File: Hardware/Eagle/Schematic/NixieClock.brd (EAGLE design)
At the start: 256.5 x 112.7 mm, 10 parts

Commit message: Molex connectors in place.. use part 39-30-6147 on mouser
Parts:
- added X1, X2, X3, X4, X5, X6: 5566-14, con-molex:5566-14
- moved U$5 23.4 mm to (-41.9, 58.4)
- moved U$6 20.5 mm to (-16.5, 58.4)
- moved U$2 19.8 mm to (74.9, 44.5)
- moved U$7 19.3 mm to (8.89, 58.4)
- moved U$4 18.9 mm to (-27.9, 45.7)
- moved U$8 18.0 mm to (34.3, 58.4)
- moved U$9 18.0 mm to (61.0, 58.4)
- moved U$10 17.8 mm to (86.4, 58.4)
- moved U$3 15.9 mm to (22.9, 44.5)
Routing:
- net N$5: track 39.9 -> 58.0 mm
- net N$8: track 195.9 -> 211.1 mm
- net N$4: track 28.6 -> 36.9 mm
- net N$6: track 65.2 -> 73.5 mm
- net N$3: track 35.6 -> 43.9 mm
- net N$1: track 47.3 -> 53.5 mm

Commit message: Replaced 14 pin connector with 12 pin... started routing
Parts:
- removed X2, X3, X4, X5, X6: 5566-14, con-molex:5566-14
- added X7: 5566-12, con-molex:5566-12
- X1: value 5566-14 -> 5566-12; device con-molex:5566-14 -> con-molex:5566-12
- moved U$2 34.5 mm to (41.9, 54.6)
- moved U$5 34.5 mm to (-74.9, 68.6)
- moved U$1 34.5 mm to (91.4, 59.7)
- moved U$10 34.5 mm to (53.3, 68.6)
- moved U$3 34.5 mm to (-10.2, 54.6)
- moved U$4 34.5 mm to (-61.0, 55.9)
- moved U$6 34.5 mm to (-49.5, 68.6)
- moved U$7 34.5 mm to (-24.1, 68.6)
- moved U$8 34.5 mm to (1.27, 68.6)
- moved U$9 34.5 mm to (27.9, 68.6)
- moved X1 14.0 mm to (-81.3, -31.8)
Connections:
- new net N$33: U$5.P$16, X7.1
- new net N$34: U$5.P$15, X7.2
- new net N$35: U$5.P$13, X7.3
- new net N$36: U$5.P$8, X7.5
- new net N$37: U$5.P$14, X7.6
- new net N$38: U$5.P$11, X7.7
- new net N$39: U$5.P$10, X7.8
- new net N$40: U$5.P$9, X7.4
- new net N$41: U$5.P$1, X7.9
- new net N$42: U$5.P$2, X7.10
- new net N$43: U$10.P$16, X1.1
- new net N$44: U$10.P$15, X1.2
- new net N$45: X1.3
- new net N$46: U$10.P$11, X1.7
- new net N$47: U$10.P$10, X1.8
- new net N$48: U$10.P$9, X1.4
- new net N$49: U$10.P$8, X1.5
- new net N$50: U$10.P$14, X1.6
- new net N$51: X1.9
- new net N$52: X1.10
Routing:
- net N$2: track 7.18 -> 5.23 mm
- net N$1: track 53.5 -> 52.4 mm

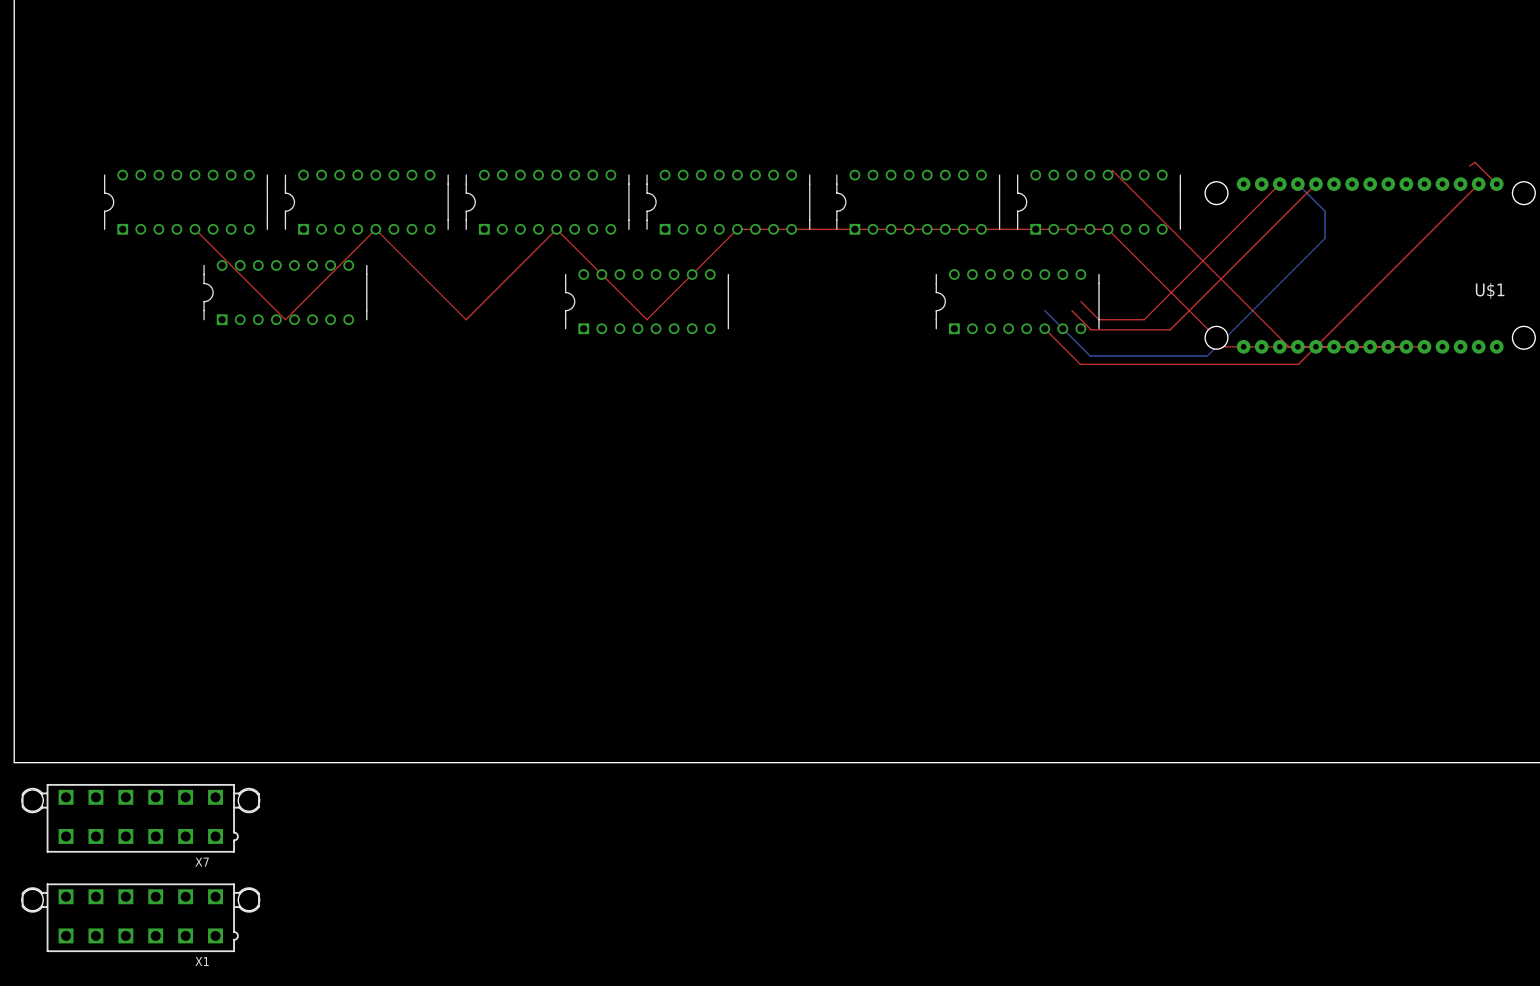
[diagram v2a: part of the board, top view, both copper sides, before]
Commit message: Made schematic a lot cleaner... pins routed from 2 driver chips to 1 SR
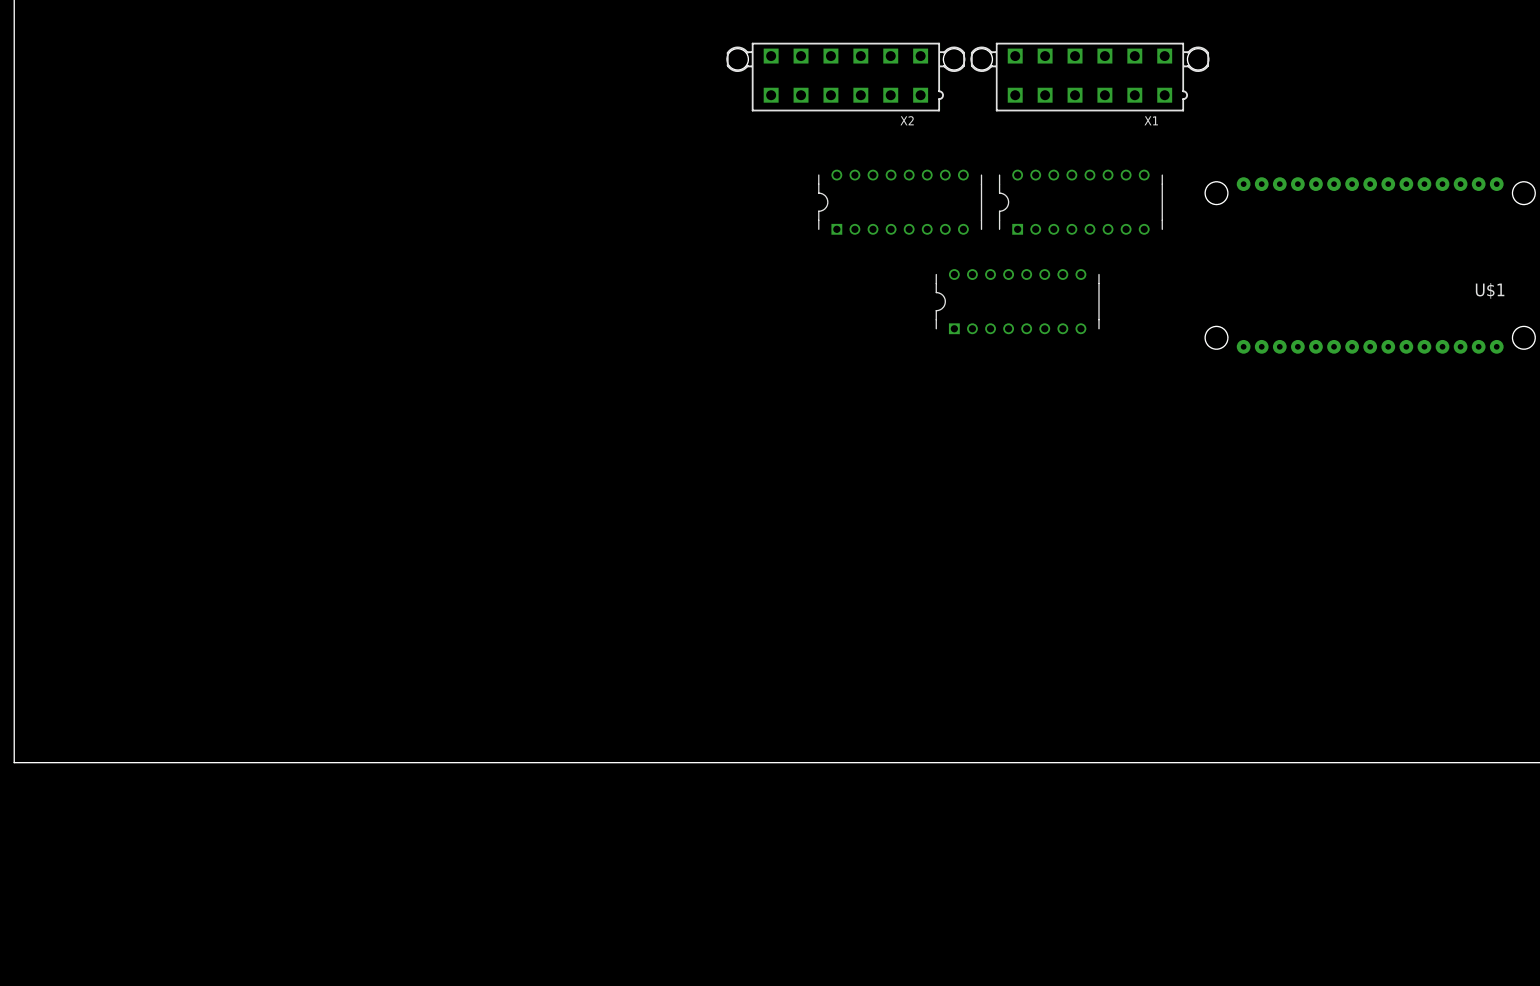
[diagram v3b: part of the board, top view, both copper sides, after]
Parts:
- removed U$3, U$4: SN74HC595NDIP-16, SN74HC595N:DIP-16
- removed U$5, U$6, U$7, U$8: DM5441ADIP-16, DM5441A:DIP-16
- removed X7: 5566-12, con-molex:5566-12
- added X2: 5566-12, con-molex:5566-12
- moved X1 178.1 mm to (52.1, 86.4)
- moved U$10 27.9 mm to (25.4, 68.6)
- moved U$9 22.9 mm to (50.8, 68.6)
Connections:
- removed net N$29: U$3.P$1, U$7.P$7
- removed net N$30: U$4.P$1, U$5.P$7
- removed net N$31: U$4.P$15, U$5.P$4
- removed net N$32: U$3.P$15, U$7.P$4
- removed net N$33: U$5.P$16, X7.1
- removed net N$34: U$5.P$15, X7.2
- removed net N$35: U$5.P$13, X7.3
- removed net N$36: U$5.P$8, X7.5
- removed net N$37: U$5.P$14, X7.6
- removed net N$38: U$5.P$11, X7.7
- removed net N$39: U$5.P$10, X7.8
- removed net N$40: U$5.P$9, X7.4
- removed net N$41: U$5.P$1, X7.9
- removed net N$42: U$5.P$2, X7.10
- removed net N$43: U$10.P$16, X1.1
- removed net N$44: U$10.P$15, X1.2
- removed net N$45: X1.3
- removed net N$46: U$10.P$11, X1.7
- removed net N$47: U$10.P$10, X1.8
- removed net N$48: U$10.P$9, X1.4
- removed net N$49: U$10.P$8, X1.5
- removed net N$50: U$10.P$14, X1.6
- removed net N$51: X1.9
- removed net N$52: X1.10
- net N$1: now also U$10.P$3, U$2.P$4; no longer U$1.GND@0, U$10.P$12, U$2.P$13, U$3.P$13, U$4.P$13, U$5.P$12, U$6.P$12, U$7.P$12, U$8.P$12, U$9.P$12
- net N$10: now also U$9.P$13, X1.3; no longer U$10.P$3, U$2.P$7
- net N$11: now also U$9.P$1, X1.9; no longer U$3.P$7, U$8.P$3
- net N$12: now also U$9.P$11, X1.7; no longer U$4.P$7, U$6.P$3
- net N$13: now also U$9.P$2, X1.10; no longer U$10.P$6, U$2.P$6
- net N$14: now also U$9.P$9, X1.4; no longer U$3.P$6, U$8.P$6
- net N$15: now also U$9.P$10, X1.8; no longer U$4.P$6, U$6.P$6
- net N$16: now also U$9.P$8, X1.5; no longer U$10.P$7, U$2.P$5
- net N$17: now also U$9.P$14, X1.6; no longer U$3.P$5, U$8.P$7
- net N$18: now also U$9.P$15, X1.2; no longer U$4.P$5, U$6.P$7
- net N$19: now also U$9.P$16, X1.1; no longer U$10.P$4, U$2.P$4
- net N$2: now also U$10.P$6, U$2.P$5; no longer U$1.3V3@2, U$2.P$10, U$2.P$16, U$3.P$10, U$3.P$16, U$4.P$10, U$4.P$16
- net N$20: now also U$10.P$11, X2.7; no longer U$3.P$4, U$8.P$4
- net N$21: now also U$10.P$9, X2.4; no longer U$4.P$4, U$6.P$4
- net N$22: now also U$10.P$10, X2.8; no longer U$2.P$3, U$9.P$3
- net N$23: now also U$10.P$8, X2.5; no longer U$3.P$3, U$7.P$3
- net N$24: now also U$10.P$14, X2.6; no longer U$4.P$3, U$5.P$3
- net N$25: now also U$10.P$15, X2.2; no longer U$2.P$2, U$9.P$6
- net N$26: now also U$10.P$16, X2.1; no longer U$3.P$2, U$7.P$6
- net N$27: now also U$10.P$2, X2.10; no longer U$4.P$2, U$5.P$6
- net N$28: now also U$10.P$1, X2.9; no longer U$2.P$1, U$9.P$7
- net N$3: now also U$2.P$16; no longer U$1.D4, U$2.P$14
- net N$4: now also U$10.P$7, U$2.P$6; no longer U$1.D2, U$2.P$11, U$3.P$11, U$4.P$11
- net N$5: now also U$10.P$4, U$2.P$7; no longer U$1.D3, U$2.P$12, U$3.P$12, U$4.P$12
- net N$6: now also U$2.P$15, U$9.P$3; no longer U$1.GND@3, U$2.P$8, U$3.P$8, U$4.P$8
- net N$7: now also U$2.P$1, U$9.P$6; no longer U$2.P$9, U$3.P$14
- net N$8: now also U$2.P$2, U$9.P$7; no longer U$1.3V3@0, U$10.P$5, U$5.P$5, U$6.P$5, U$7.P$5, U$8.P$5, U$9.P$5
- net N$9: now also U$2.P$3, U$9.P$4; no longer U$3.P$9, U$4.P$14
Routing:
- net N$8: track 211.1 -> 0.00 mm
- net N$6: track 73.5 -> 0.00 mm
- net N$5: track 58.0 -> 0.00 mm
- net N$1: track 52.4 -> 0.00 mm
- net N$3: track 43.9 -> 0.00 mm
- net N$4: track 36.9 -> 0.00 mm
- net N$2: track 5.23 -> 0.00 mm

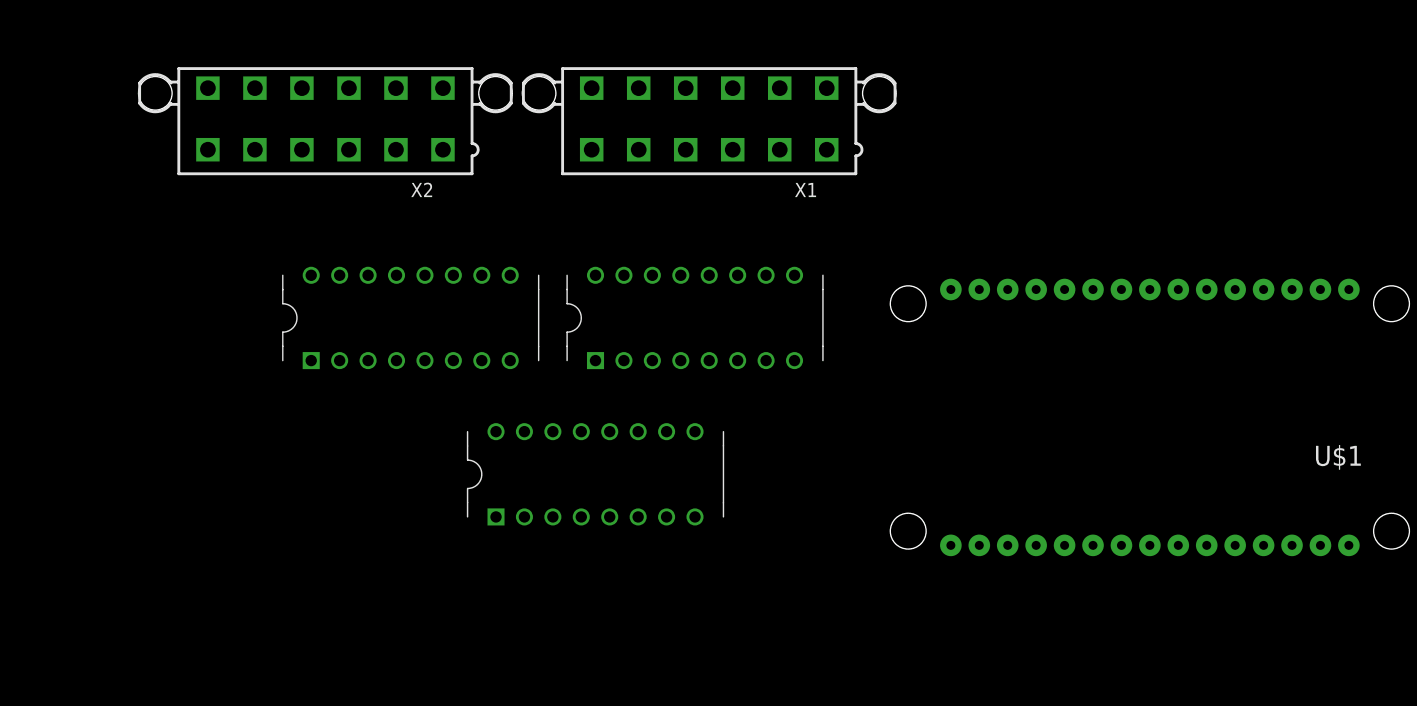
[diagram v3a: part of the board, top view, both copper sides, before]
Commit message: 2 tubes routed
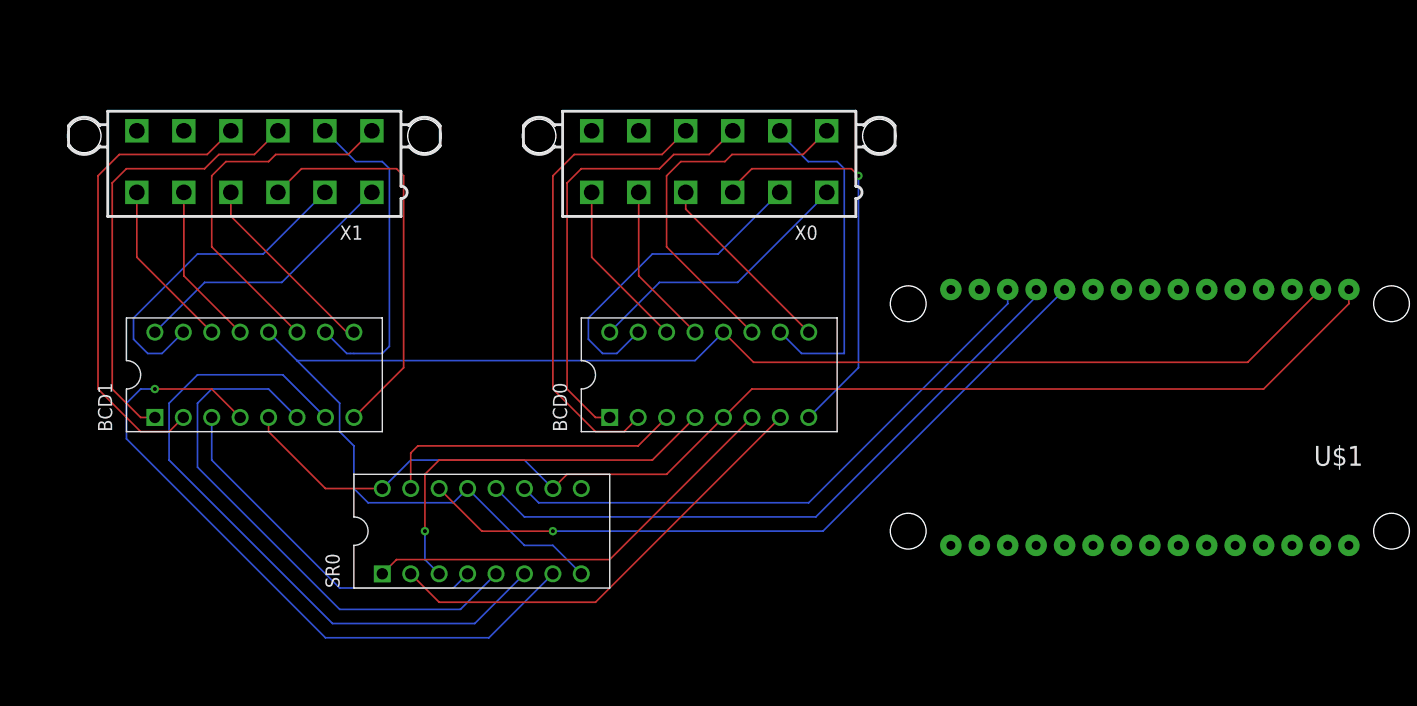
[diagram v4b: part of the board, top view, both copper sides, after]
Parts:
- removed U$10, U$9: DM5441ADIP-16, DM5441A:DIP-16
- removed U$2: SN74HC595NDIP-16, SN74HC595N:DIP-16
- removed X2: 5566-12, con-molex:5566-12
- added BCD0, BCD1: DM5441ADIP-16, DM5441A:DIP-16
- added SR0: SN74HC595NDIP-16, SN74HC595N:DIP-16
- added X0: 5566-12, con-molex:5566-12
- moved X1 40.8 mm to (11.4, 82.5)
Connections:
- removed net N$1: U$10.P$3, U$2.P$4
- removed net N$25: U$10.P$15, X2.2
- removed net N$26: U$10.P$16, X2.1
- removed net N$28: U$10.P$1, X2.9
- new net N$30: BCD1.P$8, X1.3
- new net N$31: BCD1.P$11, X1.7
- new net N$32: BCD1.P$10, X1.8
- new net N$33: BCD1.P$9, X1.4
- new net N$34: BCD1.P$2, X1.10
- new net N$35: BCD1.P$1, X1.9
- new net N$36: BCD1.P$16, X1.1
- new net N$37: BCD1.P$15, X1.2
- new net N$38: BCD1.P$14, X1.6
- new net N$39: BCD1.P$13, X1.5
- net N$10: now also BCD1.P$4, SR0.P$7; no longer U$9.P$13, X1.3
- net N$11: now also SR0.P$14, U$1.D4; no longer U$9.P$1, X1.9
- net N$12: now also BCD0.P$8, X0.3; no longer U$9.P$11, X1.7
- net N$13: now also SR0.P$12, U$1.D3; no longer U$9.P$2, X1.10
- net N$14: now also BCD0.P$11, X0.7; no longer U$9.P$9, X1.4
- net N$15: now also BCD0.P$10, X0.8; no longer U$9.P$10, X1.8
- net N$16: now also BCD0.P$9, X0.4; no longer U$9.P$8, X1.5
- net N$17: now also BCD0.P$2, X0.10; no longer U$9.P$14, X1.6
- net N$18: now also BCD0.P$1, X0.9; no longer U$9.P$15, X1.2
- net N$19: now also BCD0.P$16, X0.1; no longer U$9.P$16, X1.1
- net N$2: now also BCD0.P$5, BCD1.P$5, SR0.P$10, SR0.P$16, U$1.3V3@2; no longer U$10.P$6, U$2.P$5
- net N$20: now also BCD0.P$15, X0.2; no longer U$10.P$11, X2.7
- net N$21: now also BCD0.P$14, X0.6; no longer U$10.P$9, X2.4
- net N$22: now also BCD0.P$13, X0.5; no longer U$10.P$10, X2.8
- net N$23: now also SR0.P$11, U$1.D2; no longer U$10.P$8, X2.5
- net N$24: now also BCD0.P$12, BCD1.P$12, SR0.P$13, SR0.P$8, U$1.GND@3; no longer U$10.P$14, X2.6
- net N$27: now also SR0.P$9; no longer U$10.P$2, X2.10
- net N$3: now also BCD0.P$3, SR0.P$15; no longer U$2.P$16
- net N$4: now also BCD0.P$6, SR0.P$1; no longer U$10.P$7, U$2.P$6
- net N$5: now also BCD0.P$7, SR0.P$2; no longer U$10.P$4, U$2.P$7
- net N$6: now also BCD0.P$4, SR0.P$3; no longer U$2.P$15, U$9.P$3
- net N$7: now also BCD1.P$3, SR0.P$4; no longer U$2.P$1, U$9.P$6
- net N$8: now also BCD1.P$6, SR0.P$5; no longer U$2.P$2, U$9.P$7
- net N$9: now also BCD1.P$7, SR0.P$6; no longer U$2.P$3, U$9.P$4
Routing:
- net N$24: track 0.00 -> 138.0 mm
- net N$2: track 0.00 -> 110.1 mm
- net N$11: track 0.00 -> 66.4 mm, vias 0 -> 1
- net N$10: track 0.00 -> 62.7 mm, vias 0 -> 1
- net N$9: track 0.00 -> 61.3 mm
- net N$13: track 0.00 -> 58.1 mm
- net N$23: track 0.00 -> 52.3 mm
- net N$8: track 0.00 -> 49.4 mm
- net N$34: track 0.00 -> 42.3 mm
- net N$17: track 0.00 -> 42.3 mm
- net N$5: track 0.00 -> 40.9 mm
- net N$18: track 0.00 -> 40.0 mm
- net N$35: track 0.00 -> 40.0 mm
- net N$4: track 0.00 -> 38.8 mm
- net N$12: track 0.00 -> 36.0 mm, vias 0 -> 1
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
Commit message: Added all chips to schematic
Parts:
- added BCD2, BCD3, BCD4, BCD5: DM5441ADIP-16, DM5441A:DIP-16
- added SR1, SR2: SN74HC595NDIP-16, SN74HC595N:DIP-16
- added X2, X3, X4, X5: 5566-12, con-molex:5566-12
- moved BCD1 38.7 mm to (48.9, 73.0)
- moved SR0 38.7 mm to (69.2, 59.1)
- moved U$1 38.7 mm to (128.9, 69.2)
- moved X1 38.7 mm to (48.9, 92.1)
- moved BCD0 38.7 mm to (89.5, 73.0)
- moved X0 38.7 mm to (89.5, 92.1)
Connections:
- removed net N$2: BCD0.P$5, BCD1.P$5, SR0.P$10, SR0.P$16, U$1.3V3@2
- removed net N$24: BCD0.P$12, BCD1.P$12, SR0.P$13, SR0.P$8, U$1.GND@3
- new net N$1: BCD2.P$3, SR1.P$15
- new net N$100: BCD5.P$14, X5.6
- new net N$101: BCD5.P$13, X5.5
- new net N$25: BCD2.P$6, SR1.P$1
- new net N$26: BCD2.P$7, SR1.P$2
- new net N$28: BCD2.P$4, SR1.P$3
- new net N$29: BCD3.P$3, SR1.P$4
- new net N$40: BCD3.P$6, SR1.P$5
- new net N$41: BCD3.P$7, SR1.P$6
- new net N$42: BCD3.P$4, SR1.P$7
- new net N$43: SR0.P$11, SR1.P$11, SR2.P$11, U$1.D2
- new net N$46: SR1.P$9, SR2.P$14
- new net N$47: BCD2.P$8, X2.3
- new net N$48: BCD2.P$11, X2.7
- new net N$49: BCD2.P$10, X2.8
- new net N$50: BCD2.P$9, X2.4
- new net N$51: BCD2.P$2, X2.10
- new net N$52: BCD2.P$1, X2.9
- new net N$53: BCD2.P$16, X2.1
- new net N$54: BCD2.P$15, X2.2
- new net N$55: BCD2.P$14, X2.6
- new net N$56: BCD2.P$13, X2.5
- new net N$58: BCD3.P$8, X3.3
- new net N$59: BCD3.P$11, X3.7
- new net N$60: BCD3.P$10, X3.8
- new net N$61: BCD3.P$9, X3.4
- new net N$62: BCD3.P$2, X3.10
- new net N$63: BCD3.P$1, X3.9
- new net N$64: BCD3.P$16, X3.1
- new net N$65: BCD3.P$15, X3.2
- new net N$66: BCD3.P$14, X3.6
- new net N$67: BCD3.P$13, X3.5
- new net N$69: BCD4.P$3, SR2.P$15
- new net N$70: BCD4.P$6, SR2.P$1
- new net N$71: BCD4.P$7, SR2.P$2
- new net N$72: BCD4.P$4, SR2.P$3
- new net N$73: BCD5.P$3, SR2.P$4
- new net N$74: BCD5.P$6, SR2.P$5
- new net N$75: BCD5.P$7, SR2.P$6
- new net N$76: BCD5.P$4, SR2.P$7
- new net N$78: SR0.P$12, SR1.P$12, SR2.P$12, U$1.D3
- new net N$81: BCD4.P$8, X4.3
- new net N$82: BCD4.P$11, X4.7
- new net N$83: BCD4.P$10, X4.8
- new net N$84: BCD4.P$9, X4.4
- new net N$85: BCD4.P$2, X4.10
- new net N$86: BCD4.P$1, X4.9
- new net N$87: BCD4.P$16, X4.1
- new net N$88: BCD4.P$15, X4.2
- new net N$89: BCD4.P$14, X4.6
- new net N$90: BCD4.P$13, X4.5
- new net N$92: BCD5.P$8, X5.3
- new net N$93: BCD5.P$11, X5.7
- new net N$94: BCD5.P$10, X5.8
- new net N$95: BCD5.P$9, X5.4
- new net N$96: BCD5.P$2, X5.10
- new net N$97: BCD5.P$1, X5.9
- new net N$98: BCD5.P$16, X5.1
- new net N$99: BCD5.P$15, X5.2
- net N$13: now also BCD0.P$5, BCD1.P$5, BCD2.P$5, BCD3.P$5, BCD4.P$5, BCD5.P$5, SR0.P$10, SR0.P$16, SR1.P$10, SR1.P$16, SR2.P$10, SR2.P$16, U$1.3V3@2; no longer SR0.P$12, U$1.D3
- net N$23: now also BCD0.P$12, BCD1.P$12, BCD2.P$12, BCD3.P$12, BCD4.P$12, BCD5.P$12, SR0.P$13, SR0.P$8, SR1.P$13, SR1.P$8, SR2.P$13, SR2.P$8, U$1.GND@3; no longer SR0.P$11, U$1.D2
- net N$27: now also SR1.P$14
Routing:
- net N$24: track 138.0 -> 0.00 mm
- net N$2: track 110.1 -> 0.00 mm
- net N$23: track 52.3 -> 138.0 mm
- net N$13: track 58.1 -> 132.5 mm
- net N$78: track 0.00 -> 58.1 mm
- net N$43: track 0.00 -> 52.3 mm
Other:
- board size 256.5 x 112.7 mm -> 290.8 x 112.7 mm

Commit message: Progress
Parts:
- moved SR2 37.0 mm to (-89.5, 59.1)
- moved BCD5 25.7 mm to (-109.9, 73.0)
- moved X5 14.0 mm to (-109.9, 92.1)
- moved BCD4 13.9 mm to (-69.2, 73.0)
- moved BCD3 10.8 mm to (-30.5, 73.0)
- moved U$1 7.62 mm to (136.5, 69.2)
- moved X4 7.62 mm to (-69.2, 92.1)
- moved SR1 6.38 mm to (-10.2, 59.1)
- moved BCD2 2.54 mm to (10.2, 73.0)
- moved X3 2.54 mm to (-30.5, 92.1)
- moved X2 1.90 mm to (10.2, 92.1)
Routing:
- net N$27: track 0.00 -> 102.5 mm
- net N$78: track 58.1 -> 147.9 mm, vias 0 -> 1
- net N$43: track 52.3 -> 141.2 mm, vias 0 -> 1
- net N$23: track 138.0 -> 189.6 mm, vias 0 -> 1
- net N$13: track 132.5 -> 168.6 mm
- net N$11: track 66.4 -> 74.0 mm
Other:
- board size 290.8 x 112.7 mm -> 297.8 x 112.7 mm
